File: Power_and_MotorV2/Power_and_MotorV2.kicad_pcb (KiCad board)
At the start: 2 copper layers, 110 x 110 mm, 25 parts, among them J1 Barrel_Jack_Switch_Pin3Ring, M1 Motor_DC, Q1 BC337, Q2 BC337, SW1 SW_DPDT_x2, U1 LM317_TO-220, U2 Pin-Connector, U3 Pin-Connector, U4 Pin-Connector, U5 Pin-Connector, U6 Pin-Connector, U7 Pin-Connector

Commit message: FinalV1
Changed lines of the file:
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@@
-	)
-	(segment
-		(start 162.521434 79.821419)
-		(end 163.915343 79.821419)
-		(width 1.5)
-		(layer "B.Cu")
-		(net "GND")
 	)
 	(segment
 		(start 109.08 131.539985)
 		(end 109.08 135)
-		(width 1.5)
-		(layer "B.Cu")
-		(net "GND")
-	)
-	(segment
-		(start 167.361434 83.26751)
-		(end 167.361434 84.321419)
 		(width 1.5)
 		(layer "B.Cu")
@@
 		(start 111.361434 56.321419)
 		(end 111.361434 66.138566)
+		(width 1.5)
+		(layer "B.Cu")
+		(net "GND")
+	)
+	(segment
+		(start 164.321419 79.821419)
+		(end 167.5 83)
 		(width 1.5)
 		(layer "B.Cu")
@@
 	)
 	(segment
+		(start 162.521434 79.821419)
+		(end 164.321419 79.821419)
+		(width 1.5)
+		(layer "B.Cu")
+		(net "GND")
+	)
+	(segment
+		(start 167.5 83)
+		(end 167.5 84)
+		(width 1.5)
+		(layer "B.Cu")
+		(net "GND")
+	)
+	(segment
 		(start 109.08 136)
 		(end 116.08 143)
@@
 		(width 1.5)
 		(layer "B.Cu")
-		(net "GND")
-	)
-	(segment
-		(start 163.915343 79.821419)
-		(end 167.361434 83.26751)
-		(width 1.5)
-		(layer "B.Cu")

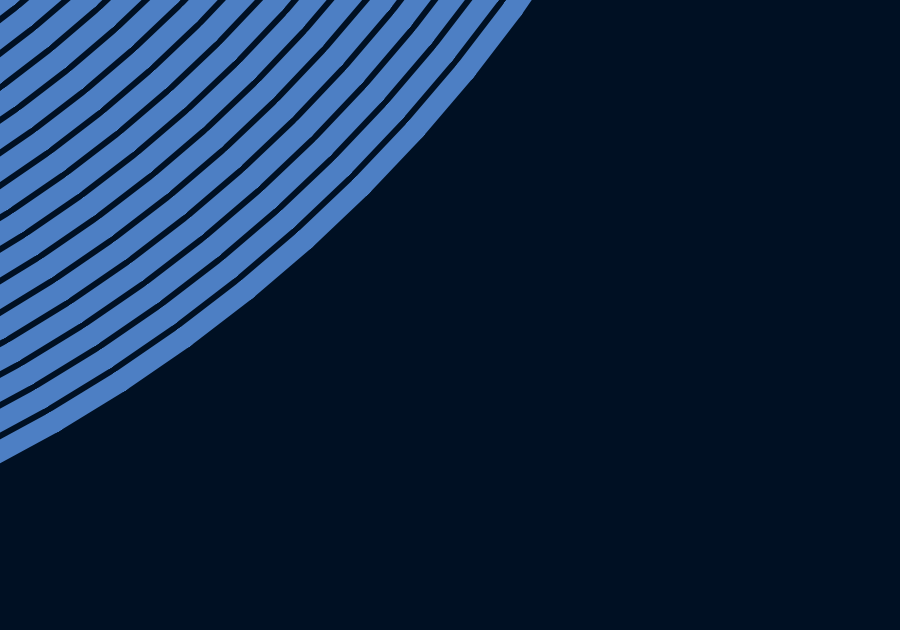
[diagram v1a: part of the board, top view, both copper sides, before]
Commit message: AddMagnet and Update Readme
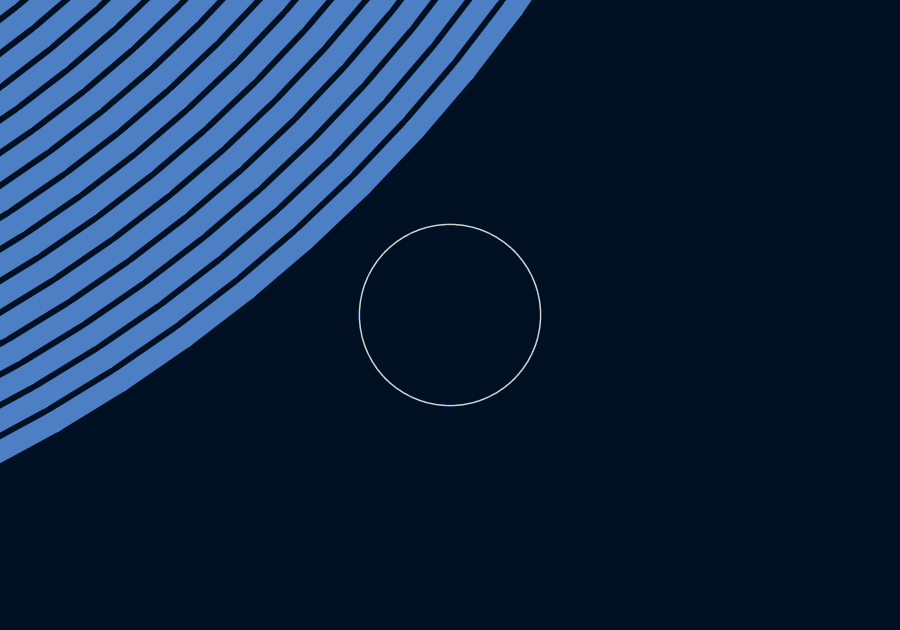
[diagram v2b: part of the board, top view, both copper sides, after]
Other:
- outline, holes or cut-outs redrawn
- board text added: "Magnet"
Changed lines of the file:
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@@
 		(layer "Edge.Cuts")
+	)
+	(gr_circle
+		(center 187.5 139)
+		(end 190.52 139)
+		(stroke
+			(width 0.05)
+			(type solid)
+		)
+		(fill no)
+		(layer "Edge.Cuts")
+	)
+	(gr_text "Magnet"
+		(at 194.5 140 45)
+		(layer "B.SilkS")
+		(effects
+			(font
+				(size 1.5 1.5)
+				(thickness 0.3)
+				(bold yes)
+			)
+			(justify left bottom mirror)
+		)
 	)
 	(segment
